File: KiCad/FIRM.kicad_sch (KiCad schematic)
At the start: 95 parts, among them J1 Conn_01x02_Pin, J3 Micro_SD_Card_Det2, J5 USB_C_Receptacle_USB2.0_16P, Q1 AO3401A, SW1 PTS815, U1 STM32F405RGTx, U2 MIC5219-3.3YM5, U7 W25Q128JVS, X2 32.768khz, Y1 12mhz

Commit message: mosfet
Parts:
- removed Q1: AO3401A, Package_TO_SOT_SMD:SOT-23, symbol Transistor_FET:AO3401A
- added Q2: IRLML6402, Package_TO_SOT_SMD:SOT-23, symbol Transistor_FET:IRLML6402
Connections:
- net VBAT: now also Q2.3 (D)
- net VBUS: now also Q2.1 (G)
- net at C22.1, D1.1 (K), U2.1 (IN)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: now also Q2.2 (S)
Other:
- moved on the sheet: R8
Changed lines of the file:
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@@
 	)
 	(junction
-		(at 245.11 201.93)
+		(at 243.84 201.93)
 		(diameter 0)
 		(color 0 0 0 0)
@@
 	)
 	(junction
-		(at 245.11 214.63)
+		(at 243.84 214.63)
 		(diameter 0)
 		(color 0 0 0 0)
@@
 	(wire
 		(pts
-			(xy 245.11 201.93) (xy 254 201.93)
+			(xy 243.84 201.93) (xy 254 201.93)
 		)
 		(stroke
@@
 	(wire
 		(pts
-			(xy 245.11 227.33) (xy 245.11 226.06)
+			(xy 243.84 227.33) (xy 243.84 226.06)
 		)
 		(stroke
@@
 	(wire
 		(pts
-			(xy 245.11 201.93) (xy 245.11 214.63)
+			(xy 243.84 201.93) (xy 243.84 214.63)
 		)
 		(stroke
@@
 	(wire
 		(pts
-			(xy 245.11 214.63) (xy 245.11 218.44)
+			(xy 243.84 214.63) (xy 243.84 218.44)
 		)
 		(stroke
@@
 	(wire
 		(pts
-			(xy 245.11 196.85) (xy 245.11 201.93)
+			(xy 243.84 196.85) (xy 243.84 201.93)
 		)
 		(stroke
@@
 	(wire
 		(pts
-			(xy 245.11 214.63) (xy 248.92 214.63)
+			(xy 243.84 214.63) (xy 248.92 214.63)
 		)
 		(stroke
@@
 	)
 	(symbol
-		(lib_id "Transistor_FET:AO3401A")
-		(at 259.08 201.93 0)
-		(unit 1)
-		(exclude_from_sim no)
-		(in_bom yes)
-		(on_board yes)
-		(dnp no)
-		(fields_autoplaced yes)
-		(property "Reference" "Q1"
-			(at 265.43 200.6599 0)
-			(effects
-				(font
-					(size 1.27 1.27)
-				)
-				(justify left)
-			)
-		)
-		(property "Value" "AO3401A"
-			(at 265.43 203.1999 0)
-			(effects
-				(font
-					(size 1.27 1.27)
-				)
-				(justify left)
-			)
-		)
-		(property "Footprint" "Package_TO_SOT_SMD:SOT-23"
-			(at 264.16 203.835 0)
-			(effects
-				(font
-					(size 1.27 1.27)
-					(italic yes)
-				)
-				(justify left)
-				(hide yes)
-			)
-		)
-		(property "Datasheet" "http://www.aosmd.com/pdfs/datasheet/AO3401A.pdf"
-			(at 264.16 205.74 0)
-			(effects
-				(font
-					(size 1.27 1.27)
-				)
-				(justify left)
-				(hide yes)
-			)
-		)
-		(property "Description" "-4.0A Id, -30V Vds, P-Channel MOSFET, SOT-23"
-			(at 259.08 201.93 0)
-			(effects
-				(font
-					(size 1.27 1.27)
-				)
-				(hide yes)
-			)
-		)
-		(pin "1"
-		)
-		(pin "3"
-		)
-		(pin "2"
-		)
-		(instances
-			(project ""
-				(path "/d3f8a00a-ef65-439d-87f3-373a106a7ddb"
-					(reference "Q1")
-					(unit 1)
-				)
-			)
-		)
-	)
-	(symbol
 		(lib_id "power:GND")
 		(at 35.56 71.12 0)
@@
 	(symbol
 		(lib_id "power:VBUS")
-		(at 245.11 196.85 0)
+		(at 243.84 196.85 0)
 		(unit 1)
 		(exclude_from_sim no)
@@
 		(dnp no)
 		(property "Reference" "#PWR037"
-			(at 245.11 200.66 0)
+			(at 243.84 200.66 0)
 			(effects
 				(font
@@
 		)
 		(property "Value" "VBUS"
-			(at 244.856 192.532 0)
+			(at 243.586 192.532 0)
 			(effects
 				(font
@@
 		)
 		(property "Footprint" ""
-			(at 245.11 196.85 0)
+			(at 243.84 196.85 0)
 			(effects
 				(font
@@
 		)
 		(property "Datasheet" ""
-			(at 245.11 196.85 0)
+			(at 243.84 196.85 0)
 			(effects
 				(font
@@
 		)
 		(property "Description" "Power symbol creates a global label with name \"VBUS\""
-			(at 245.11 196.85 0)
+			(at 243.84 196.85 0)
 			(effects
 				(font
@@
 	(symbol
 		(lib_id "Device:R")
-		(at 245.11 222.25 0)
+		(at 243.84 222.25 0)
 		(unit 1)
 		(exclude_from_sim no)
@@
 		(dnp no)
 		(property "Reference" "R8"
-			(at 246.888 220.726 0)
+			(at 245.618 220.726 0)
 			(effects
 				(font
@@
 		)
 		(property "Value" "100k"
-			(at 247.142 223.52 0)
+			(at 245.872 223.52 0)
 			(effects
 				(font
@@
 		)
 		(property "Footprint" ""
-			(at 243.332 222.25 90)
+			(at 242.062 222.25 90)
 			(effects
 				(font
@@
 		)
 		(property "Datasheet" "~"
-			(at 245.11 222.25 0)
+			(at 243.84 222.25 0)
 			(effects
 				(font
@@
 		)
 		(property "Description" "Resistor"
-			(at 245.11 222.25 0)
+			(at 243.84 222.25 0)
 			(effects
 				(font
@@
 		(on_board yes)
 		(dnp no)
-		(fields_autoplaced yes)
 		(property "Reference" "D1"
 			(at 253.0475 208.28 0)
@@
 			)
 		)
-		(property "Datasheet" "~"
+		(property "Datasheet" "https://www.diodes.com/assets/Datasheets/1N5819HW.pdf"
 			(at 252.73 214.63 0)
 			(effects
@@
 			)
 		)
-		(property "Description" "Schottky diode"
-			(at 252.73 214.63 0)
+		(property "Description" "1N5819HW-7-F"
+			(at 252.73 217.17 0)
 			(effects
 				(font
 					(size 1.27 1.27)
 				)
-				(hide yes)
 			)
 		)
@@
 	(symbol
 		(lib_id "power:GND")
-		(at 245.11 227.33 0)
+		(at 243.84 227.33 0)
 		(unit 1)
 		(exclude_from_sim no)
@@
 		(fields_autoplaced yes)
 		(property "Reference" "#PWR028"
-			(at 245.11 233.68 0)
+			(at 243.84 233.68 0)
 			(effects
 				(font
@@
 		)
 		(property "Value" "GND"
-			(at 245.11 232.41 0)
+			(at 243.84 232.41 0)
 			(effects
 				(font
@@
 		)
 		(property "Footprint" ""
-			(at 245.11 227.33 0)
+			(at 243.84 227.33 0)
 			(effects
 				(font
@@
 		)
 		(property "Datasheet" ""
-			(at 245.11 227.33 0)
+			(at 243.84 227.33 0)
 			(effects
 				(font
@@
 		)
 		(property "Description" "Power symbol creates a global label with name \"GND\" , ground"
-			(at 245.11 227.33 0)
+			(at 243.84 227.33 0)
 			(effects
 				(font
@@
 					(unit 1)
 				)
+			)
+		)
+	)
+	(symbol
+		(lib_id "Transistor_FET:IRLML6402")
+		(at 259.08 201.93 0)
+		(unit 1)
+		(exclude_from_sim no)
+		(in_bom yes)
+		(on_board yes)
+		(dnp no)
+		(fields_autoplaced yes)
+		(property "Reference" "Q2"
+			(at 265.43 200.6599 0)
+			(effects
+				(font
+					(size 1.27 1.27)
+				)
+				(justify left)
+			)
+		)
+		(property "Value" "IRLML6402"
+			(at 265.43 203.1999 0)
+			(effects
+				(font
+					(size 1.27 1.27)
+				)
+				(justify left)
+			)
+		)
+		(property "Footprint" "Package_TO_SOT_SMD:SOT-23"
+			(at 264.16 203.835 0)
+			(effects
+				(font
+					(size 1.27 1.27)
+					(italic yes)
+				)
+				(justify left)
+				(hide yes)
+			)
+		)
+		(property "Datasheet" "https://www.infineon.com/dgdl/irlml6402pbf.pdf?fileId=5546d462533600a401535668d5c2263c"
+			(at 264.16 205.74 0)
+			(effects
+				(font
+					(size 1.27 1.27)
+				)
+				(justify left)
+				(hide yes)
+			)
+		)
+		(property "Description" "-3.7A Id, -20V Vds, 65mOhm Rds, P-Channel HEXFET Power MOSFET, SOT-23"
+			(at 259.08 201.93 0)
+			(effects
+				(font
+					(size 1.27 1.27)
+				)
+				(hide yes)
+			)
+		)
+		(pin "3"
+		)
+		(pin "1"
+		)
+		(pin "2"
+		)
+		(instances
+			(project ""
+				(path "/d3f8a00a-ef65-439d-87f3-373a106a7ddb"
+					(reference "Q2")
+					(unit 1)
+				)

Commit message: footprints and start pcb
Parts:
- C1, C10, C11, C12, C13, C14, C15, C16, C17, C18, C19, C2, C20, C21, C22, C23, C24, C25, C26, C27, C3, C4, C5, C6, C7, C8, C9: footprint (none) -> Capacitor_SMD:C_1206_3216Metric
- D1: footprint (none) -> Diode_SMD:D_SOD-123
- D2, D3, D4, D5: footprint (none) -> LED_SMD:LED_0805_2012Metric
- FB1: footprint (none) -> Inductor_SMD:L_1206_3216Metric
- J1: footprint (none) -> Connector_PinHeader_2.54mm:PinHeader_1x02_P2.54mm_Vertical
- J3: footprint (none) -> Connector_Card:microSD_HC_Hirose_DM3BT-DSF-PEJS
- J5: footprint (none) -> Connector_USB:USB_C_Receptacle_Amphenol_124019772112A
- JP1, JP2, JP3, JP4: footprint (none) -> Jumper:SolderJumper-2_P1.3mm_Open_RoundedPad1.0x1.5mm
- R1, R10, R11, R12, R13, R14, R15, R16, R17, R18, R19, R2, R20, R21, R3, R4, R5, R6, R7, R8: footprint (none) -> Resistor_SMD:R_1206_3216Metric
- SW1: footprint (none) -> Button_Switch_SMD:SW_SPST_PTS810
- TP1, TP10, TP11, TP12, TP13, TP14, TP15, TP16, TP17, TP18, TP2, TP24, TP26, TP27, TP28, TP29, TP3, TP30, TP4, TP5, TP6, TP7, TP8, TP9: footprint (none) -> TestPoint:TestPoint_THTPad_2.5x2.5mm_Drill1.2mm
- TP25: footprint (none) -> TestPoint:TestPoint_Pad_2.0x2.0mm
- X2: footprint (none) -> Crystal:Crystal_SMD_3215-2Pin_3.2x1.5mm
- Y1: footprint (none) -> Crystal:Crystal_SMD_3225-4Pin_3.2x2.5mm

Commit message: changing some sizes
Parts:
- C1, C10, C11, C12, C13, C14, C15, C16, C17, C18, C19, C2, C20, C21, C22, C23, C24, C25, C26, C27, C3, C4, C5, C6, C7, C8, C9: footprint Capacitor_SMD:C_1206_3216Metric -> Capacitor_SMD:C_0603_1608Metric
- R1, R10, R11, R12, R13, R14, R15, R16, R17, R18, R19, R2, R20, R21, R3, R4, R5, R6, R7, R8: footprint Resistor_SMD:R_1206_3216Metric -> Resistor_SMD:R_0603_1608Metric
- TP1, TP10, TP11, TP12, TP13, TP14, TP15, TP16, TP17, TP18, TP2, TP24, TP26, TP27, TP28, TP29, TP3, TP30, TP4, TP5, TP6, TP7, TP8, TP9: footprint TestPoint:TestPoint_THTPad_2.5x2.5mm_Drill1.2mm -> TestPoint:TestPoint_THTPad_1.5x1.5mm_Drill0.7mm
- TP25: footprint TestPoint:TestPoint_Pad_2.0x2.0mm -> TestPoint:TestPoint_Pad_1.5x1.5mm

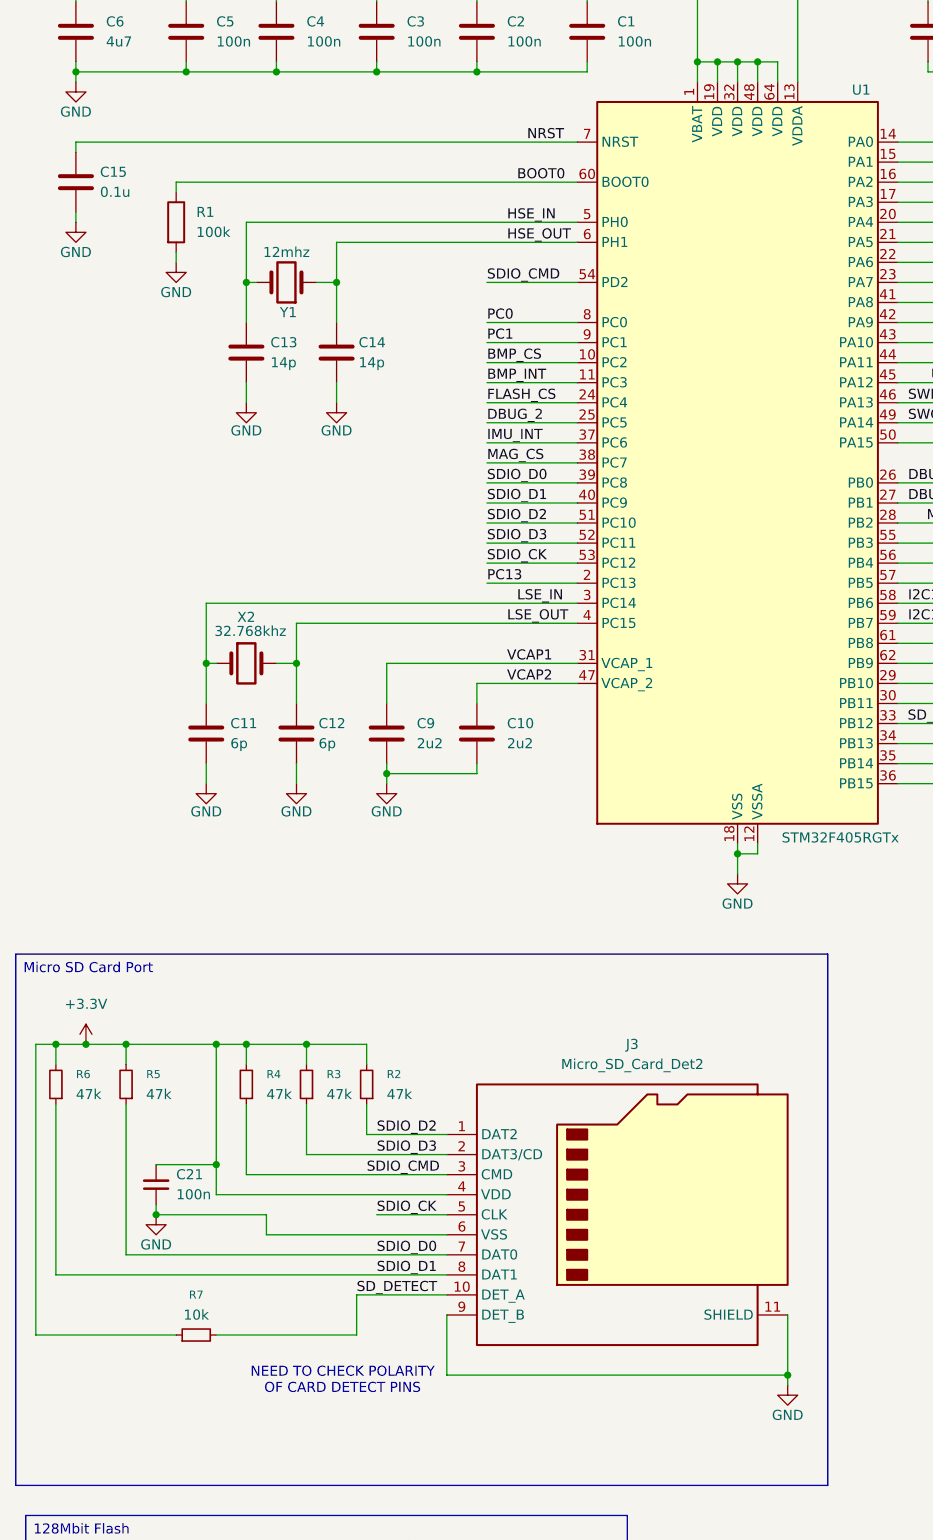
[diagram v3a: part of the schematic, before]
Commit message: update crystal and sd card port
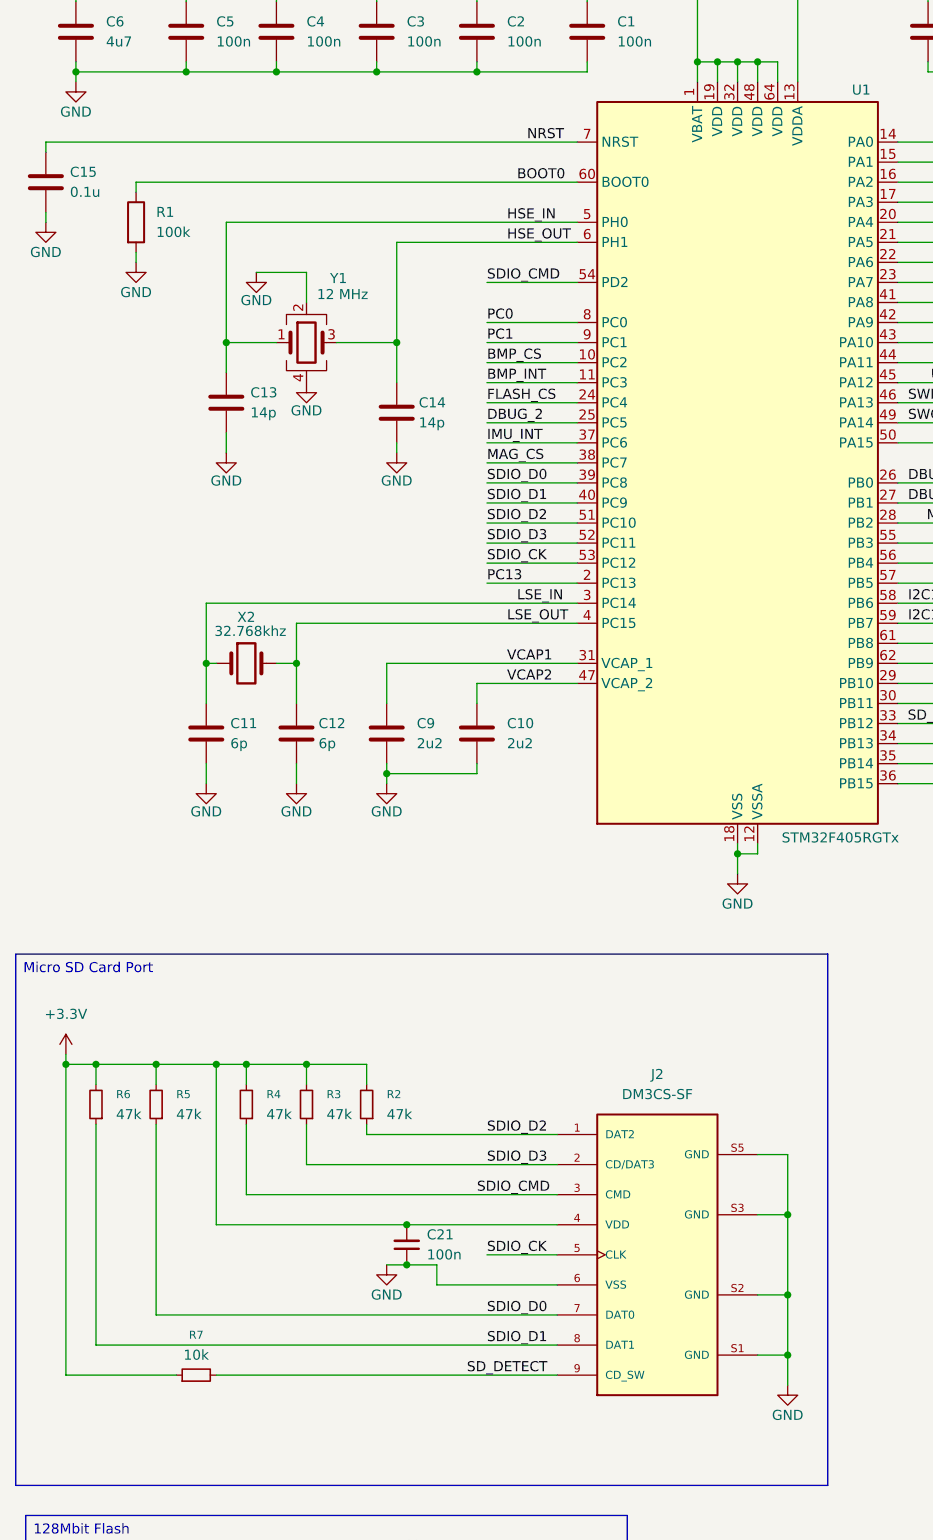
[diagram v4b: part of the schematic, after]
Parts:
- removed J3: Micro_SD_Card_Det2, Connector_Card:microSD_HC_Hirose_DM3BT-DSF-PEJS, symbol Connector:Micro_SD_Card_Det2
- removed Y1: 12mhz, Crystal:Crystal_SMD_3225-4Pin_3.2x2.5mm, symbol Device:Crystal
- added J2: DM3CS-SF, DM3CS-SF:HRS_DM3CS-SF, symbol DM3CS-SF:DM3CS-SF
- added Y1: 12 MHz, Crystal:Crystal_SMD_Abracon_ABM8G-4Pin_3.2x2.5mm, symbol Device:Crystal_GND24
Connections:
- net +3.3V: now also J2.4 (VDD)
- net GND: now also J2.6 (VSS), J2.S1 (GND), J2.S2 (GND), J2.S3 (GND), J2.S5 (GND), Y1.2, Y1.4
- net HSE_IN: now also Y1.1
- net HSE_OUT: now also Y1.3
- net SDIO_CK: now also J2.5 (CLK)
- net SDIO_CMD: now also J2.3 (CMD)
- net SDIO_D0: now also J2.7 (DAT0)
- net SDIO_D1: now also J2.8 (DAT1)
- net SDIO_D2: now also J2.1 (DAT2)
- net SDIO_D3: now also J2.2 (CD/DAT3)
- net SD_DETECT: now also J2.9 (CD_SW)
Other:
- note removed: "NEED TO CHECK POLARITY OF CARD DETECT PINS"
- moved on the sheet: C13, C14, C15, C21, R1, R2, R3, R4, R5, R6, R7

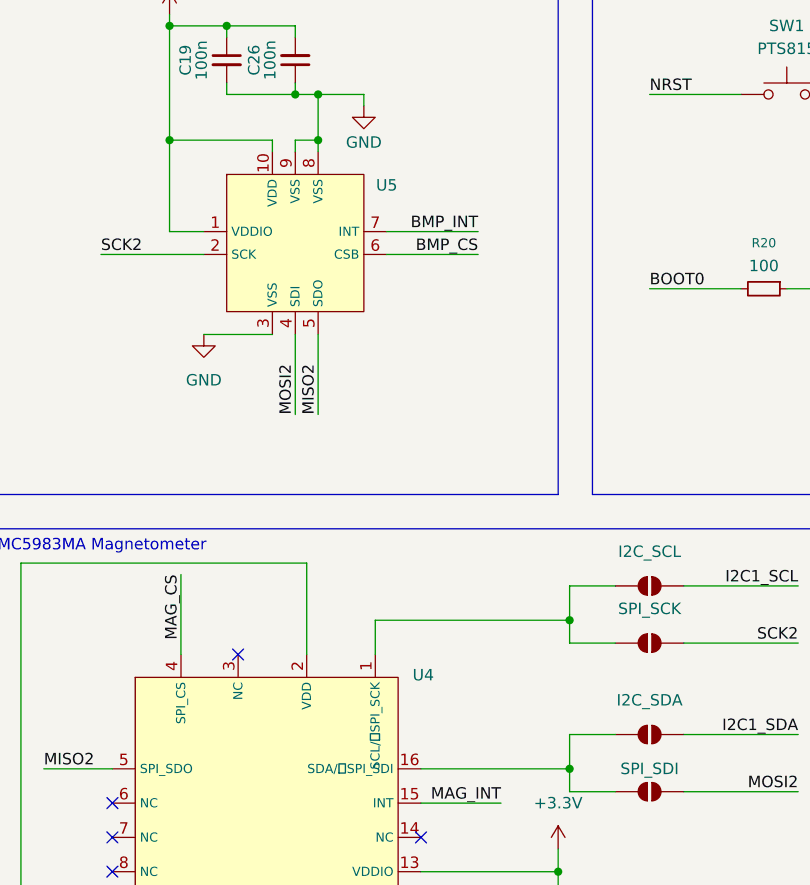
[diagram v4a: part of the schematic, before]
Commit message: Use project library instead of global library
Also reorganize footprints, custom symbols, and 3d models. Updated README about using KiCad in the project.
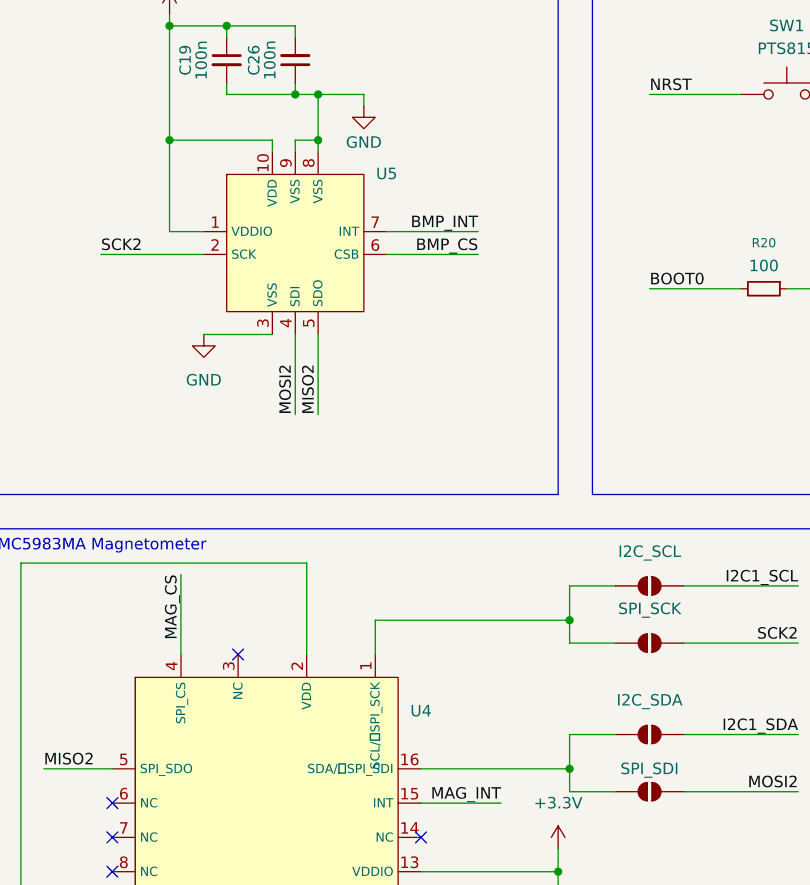
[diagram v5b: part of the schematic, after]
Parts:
- J2: symbol DM3CS-SF:DM3CS-SF -> connectors:DM3CS-SF
- U3: symbol Sensor_Motion:ICM-45686 -> sensors:ICM-45686
- U4: symbol Sensor_Magnetic:MMC5983MA -> sensors:MMC5983MA
- U5: symbol Sensor_Pressure:BMP581 -> sensors:BMP581
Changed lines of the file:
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@@
 	)
 	(symbol
-		(lib_id "Sensor_Magnetic:MMC5983MA")
+		(lib_id "sensors:MMC5983MA")
 		(at 325.12 111.76 0)
 		(unit 1)
@@
 		(fields_autoplaced yes)
 		(property "Reference" "U4"
-			(at 341.884 96.266 0)
+			(at 341.63 100.2598 0)
 			(effects
 				(font
@@
 		)
 		(property "Value" "~"
-			(at 341.884 98.044 0)
+			(at 341.63 102.7998 0)
 			(effects
 				(font
@@
 			)
 		)
-		(property "Datasheet" ""
+		(property "Datasheet" "https://media.digikey.com/pdf/Data%20Sheets/MEMSIC%20PDFs/MMC5983MA_RevA_4-3-19.pdf"
 			(at 325.12 111.76 0)
 			(effects
@@
 			)
 		)
-		(property "Description" ""
+		(property "Description" "Magnetometer"
 			(at 325.12 111.76 0)
 			(effects
@@
 	)
 	(symbol
-		(lib_id "Sensor_Pressure:BMP581")
+		(lib_id "sensors:BMP581")
 		(at 327.66 48.26 0)
 		(unit 1)
@@
 		(fields_autoplaced yes)
 		(property "Reference" "U5"
-			(at 337.82 41.8398 0)
+			(at 337.82 40.5698 0)
 			(effects
 				(font
@@
 		)
 		(property "Value" "~"
-			(at 337.82 43.7449 0)
+			(at 337.82 43.1098 0)
 			(effects
 				(font
@@
 			)
 		)
-		(property "Datasheet" ""
+		(property "Datasheet" "https://www.bosch-sensortec.com/media/boschsensortec/downloads/datasheets/bst-bmp581-ds004.pdf"
 			(at 327.66 48.26 0)
 			(effects
@@
 			)
 		)
-		(property "Description" ""
+		(property "Description" "Bosch Pressure Sensor"
 			(at 327.66 48.26 0)
 			(effects
@@
 	)
 	(symbol
-		(lib_id "Sensor_Motion:ICM-45686")
+		(lib_id "sensors:ICM-45686")
 		(at 251.46 55.88 0)
 		(unit 1)
@@
 			)
 		)
-		(property "Datasheet" ""
+		(property "Datasheet" "https://www.mouser.com/catalog/specsheets/TDK_DS_000577_ICM_45686.pdf?srsltid=AfmBOooJ55_Jsy4PB-5CLV5vQtmUmcbglSfWs9S-cLOBSOXLc19UPaWf"
 			(at 251.46 55.88 0)
 			(effects
@@
 			)
 		)
-		(property "Description" ""
+		(property "Description" "6 Axis IMU (Acceleration + Gyroscope)"
 			(at 251.46 55.88 0)
 			(effects
@@
 	)
 	(symbol
-		(lib_id "DM3CS-SF:DM3CS-SF")
+		(lib_id "connectors:DM3CS-SF")
 		(at 96.52 196.85 0)
 		(unit 1)
